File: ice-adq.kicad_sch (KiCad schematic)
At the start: 0 parts

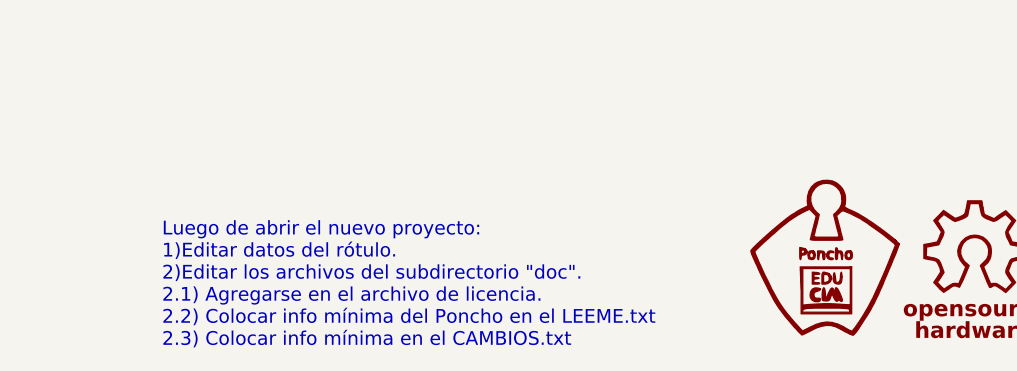
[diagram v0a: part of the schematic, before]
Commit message: Actualizacion a kicad 7, seleccion de ganancia de la etapa de amplificacion de presion de aceite.
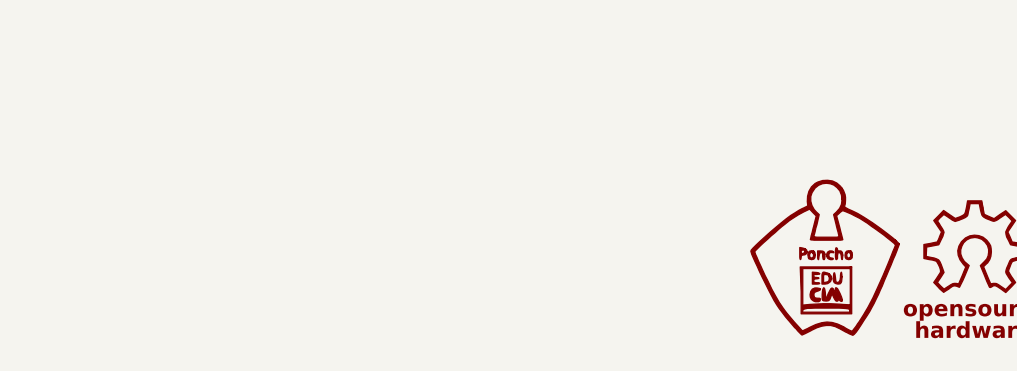
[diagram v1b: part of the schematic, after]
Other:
- note removed: "Luego de abrir el nuevo proyecto: 1)Editar datos del rótulo. 2)Editar los archivos del subdirectorio "doc". 2.1) Agregarse en el archivo de licencia. 2.2) Colocar info mínima del Poncho en el LEEME.txt 2.3) Colocar info mínima en el CAMBIOS.txt"
